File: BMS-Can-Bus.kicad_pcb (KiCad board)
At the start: 2 copper layers, 127.7 x 130.5 mm, 59 parts, among them J1 Conn_01x05, J2 Conn_01x02, J3 bat+, Q1 dfsg1, Q2 dsg2, Q3 Q_PMOS_GSD, Q4 Q_PMOS_GSD, Q5 Q_PMOS_GSD, Q6 Q_PMOS_GSD, Q7 chg1, Q8 chg2, U1 BQ76952PFB, U2 STM32F103C8Tx, U4 SN65HVD230

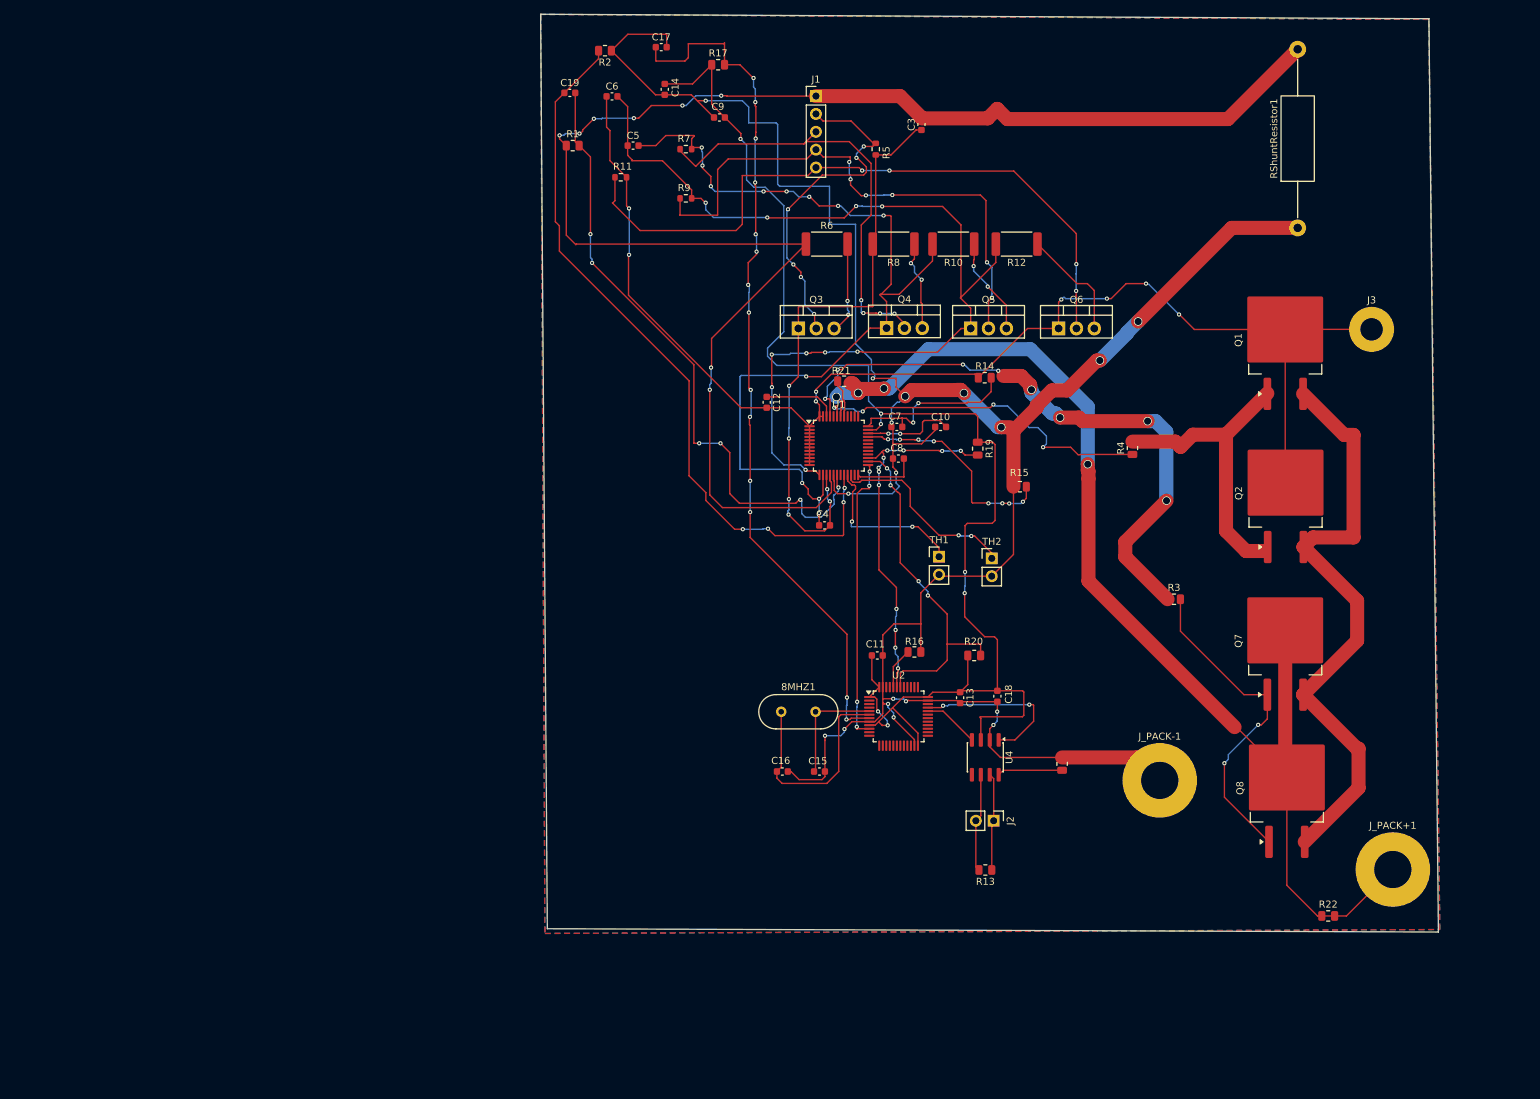
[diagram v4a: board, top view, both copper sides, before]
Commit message: refactor(pcb): reduce board size and increase power trace widths to 2mm
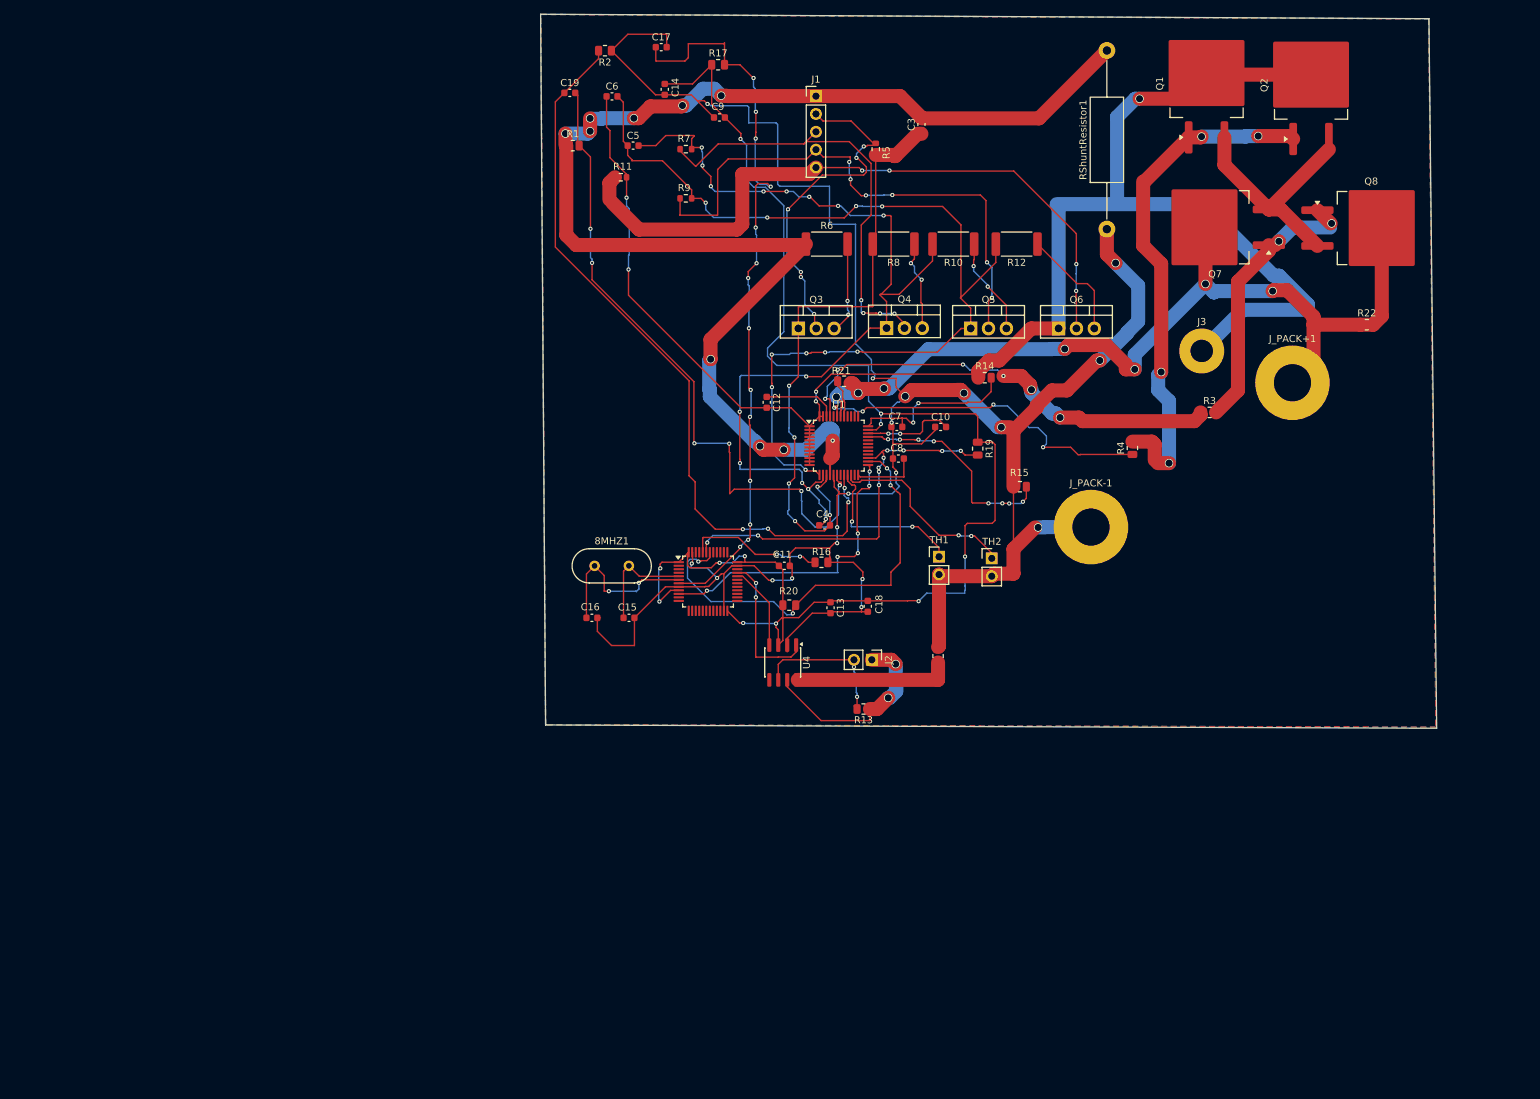
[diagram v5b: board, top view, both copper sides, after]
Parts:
- moved R22 84.3 mm to (215.8, 56.5)
- moved Q8 80.5 mm to (216.5, 42.7), turned to 0 degrees
- moved J_PACK+1 70.7 mm to (205.3, 64.7)
- moved Q7 59.7 mm to (194.2, 42.6), turned to 180 degrees
- moved Q2 58.1 mm to (207.9, 22.4)
- moved Q1 38.1 mm to (193.0, 22.2)
- moved J_PACK-1 37.3 mm to (176.6, 85.2)
- moved C15 34.8 mm to (110.9, 98.1)
- moved C16 34.8 mm to (105.6, 98.1)
- moved 8MHZ1 33.7 mm to (106.0, 90.8)
- moved U2 33.2 mm to (122.2, 93.0)
- moved U4 31.8 mm to (132.8, 104.5)
- moved J2 28.7 mm to (145.4, 104.1)
- moved R13 28.7 mm to (144.3, 111.1)
- moved R20 27.3 mm to (133.7, 96.3)
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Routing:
- net Net-(Q1-S): track 86.8 -> 35.5 mm
- net Net-(J3-Pin_1): track 186.5 -> 234.9 mm, vias 8 -> 5
- net Net-(J_PACK+1-Pin_1): track 167.8 -> 127.8 mm, vias 4 -> 7
- net Net-(J1-Pin_1): track 226.3 -> 192.1 mm, vias 8 -> 10
- net Net-(Q1-D): track 43.7 -> 73.9 mm, vias 0 -> 4
- net Net-(U1-CHG): track 88.3 -> 64.5 mm, vias 8 -> 6
- net Net-(U2-NRST): track 123.4 -> 105.6 mm
- net Net-(J2-Pin_1): track 13.9 -> 29.1 mm, vias 0 -> 2
- net Net-(U2-BOOT0): track 5.86 -> 19.5 mm, vias 0 -> 2
- net Net-(U4-Rs): track 9.28 -> 22.4 mm
- net /I2C_SCL: track 49.9 -> 61.2 mm
- net Net-(U2-PD1): track 31.8 -> 23.9 mm, vias 0 -> 2
- net Net-(J2-Pin_2): track 14.0 -> 21.0 mm, vias 0 -> 2
- net Net-(Q7-D): track 47.0 -> 40.1 mm
- net Net-(U1-SRP): track 91.4 -> 95.8 mm
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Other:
- board size 127.7 x 130.5 mm -> 127.4 x 101.5 mm
